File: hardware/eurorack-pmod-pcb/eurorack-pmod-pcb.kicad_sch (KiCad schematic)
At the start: 2 parts

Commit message: Finish schematic with AK4619, need to decide on other features
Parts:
- added C? (x2): 2u2, symbol Device:C_Polarized_Small
- added C? (x3): 10u, symbol Device:C_Polarized_Small
- added C? (x8): 1u, symbol Device:C_Polarized_Small
- added C? (x3): 100n, symbol Device:C_Small
- added J? (x7): PJ301BM, AudioJacks:Jack_3.5mm_QingPu_WQP-PJ301BM_Vertical, symbol Connector:AudioJack2_SwitchT
- added J?: PMOD_CONN, symbol Connector_Generic:Conn_02x06_Top_Bottom
- added JP?: OPEN, symbol Jumper:SolderJumper_2_Open
- added R? (x4): 33K, symbol Device:R
- added R? (x4): 68K, symbol Device:R
- added R? (x3): 4K7, symbol Device:R
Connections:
- net GND: now reaches J?.S
- net GND: now also U?.19 (VSS1), U?.2 (SDIN2), U?.20 (VREFL), U?.29 (SI), U?.33 (PAD), U?.4 (VSS2), C?.2, C?.2, C?.2, C?.2, C?.2, C?.2, C?.2, C?.2, J?.11 (Pin_11), J?.5 (Pin_5), J?.S, J?.S, J?.S, J?.S, J?.S, J?.S, J?.S, R?.2, R?.2, R?.2, R?.2, R?.2
- net at J?.T: now also R?.1
- net SDIN1: now reaches U?.1 (SDIN1)
- net SDIN1: now also J?.1 (Pin_1)
- net IN4_AUDIO_AC: now reaches U?.10 (IN4P/AIN4R/AIN6R)
- net IN4_AUDIO_AC: now also C?.1
- net IN3_AUDIO_AC: now reaches U?.12 (IN3P/AIN4L/AIN6L)
- net IN3_AUDIO_AC: now also C?.1
- net IN2_AUDIO_AC: now reaches U?.14 (IN2P/AIN1R/AIN3R)
- net IN2_AUDIO_AC: now also C?.1
- net IN1_AUDIO_AC: now reaches U?.16 (IN1P/AIN1L/AIN3L)
- net IN1_AUDIO_AC: now also C?.1
- net at U?.17 (VCOM): now also C?.1
- net +3V3: now reaches U?.18 (AVDD)
- net +3V3: now also U?.21 (VREFH), U?.3 (TVDD), C?.1, C?.1, C?.1, C?.1, C?.1, C?.1, J?.12 (Pin_12), J?.6 (Pin_6), JP?.1 (A), R?.1, R?.1
- net at U?.22 (AOUT1L): now also C?.2
- net at U?.23 (AOUT1R): now also C?.2
- net at U?.24 (AOUT2L): now also C?.2
- net at U?.25 (AOUT2R): now also C?.2
- net PDN: now reaches U?.26 (PDN)
- net PDN: now also J?.9 (Pin_9)
- net at U?.27 (CAD/~{CS}): now also JP?.2 (B), R?.1
- net SCL: now reaches U?.28 (SCL/SCLK)
- net SCL: now also J?.7 (Pin_7), R?.2
- net SDA: now reaches U?.30 (SDA/SO)
- net SDA: now also J?.8 (Pin_8), R?.2
- net SDOUT1: now reaches U?.31 (SDOUT1)
- net SDOUT1: now also J?.2 (Pin_2)
- net at U?.5 (AVDRV): now also C?.1
- net LRCK: now reaches U?.6 (LRCK)
- net LRCK: now also J?.3 (Pin_3)
- net BICK: now reaches U?.7 (BICK)
- net BICK: now also J?.4 (Pin_4)
- net MCLK: now reaches U?.8 (MCLK)
- net MCLK: now also J?.10 (Pin_10)
- new net: J?.T, R?.1 (x3)
- new net: C?.2, R?.1, R?.2 (x4)
- new net: C?.1, J?.T (x4)
- no-connect marks 0 -> 9
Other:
- moved on the sheet: J?, U?

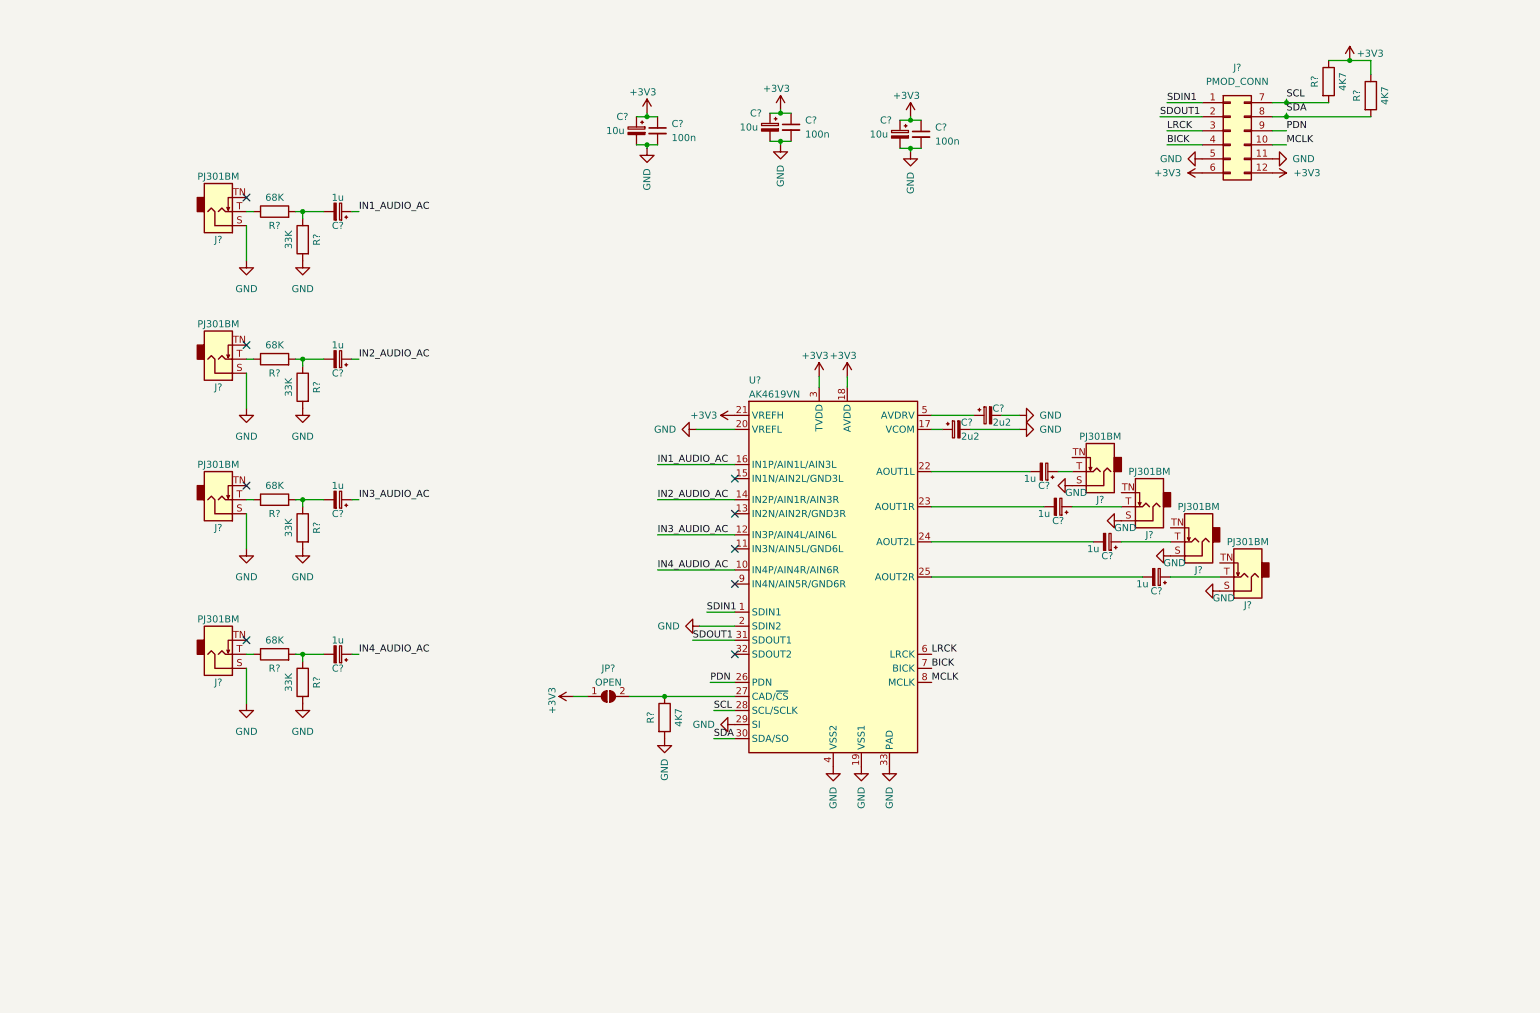
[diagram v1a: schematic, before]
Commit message: Finish input/output stages around AK4619
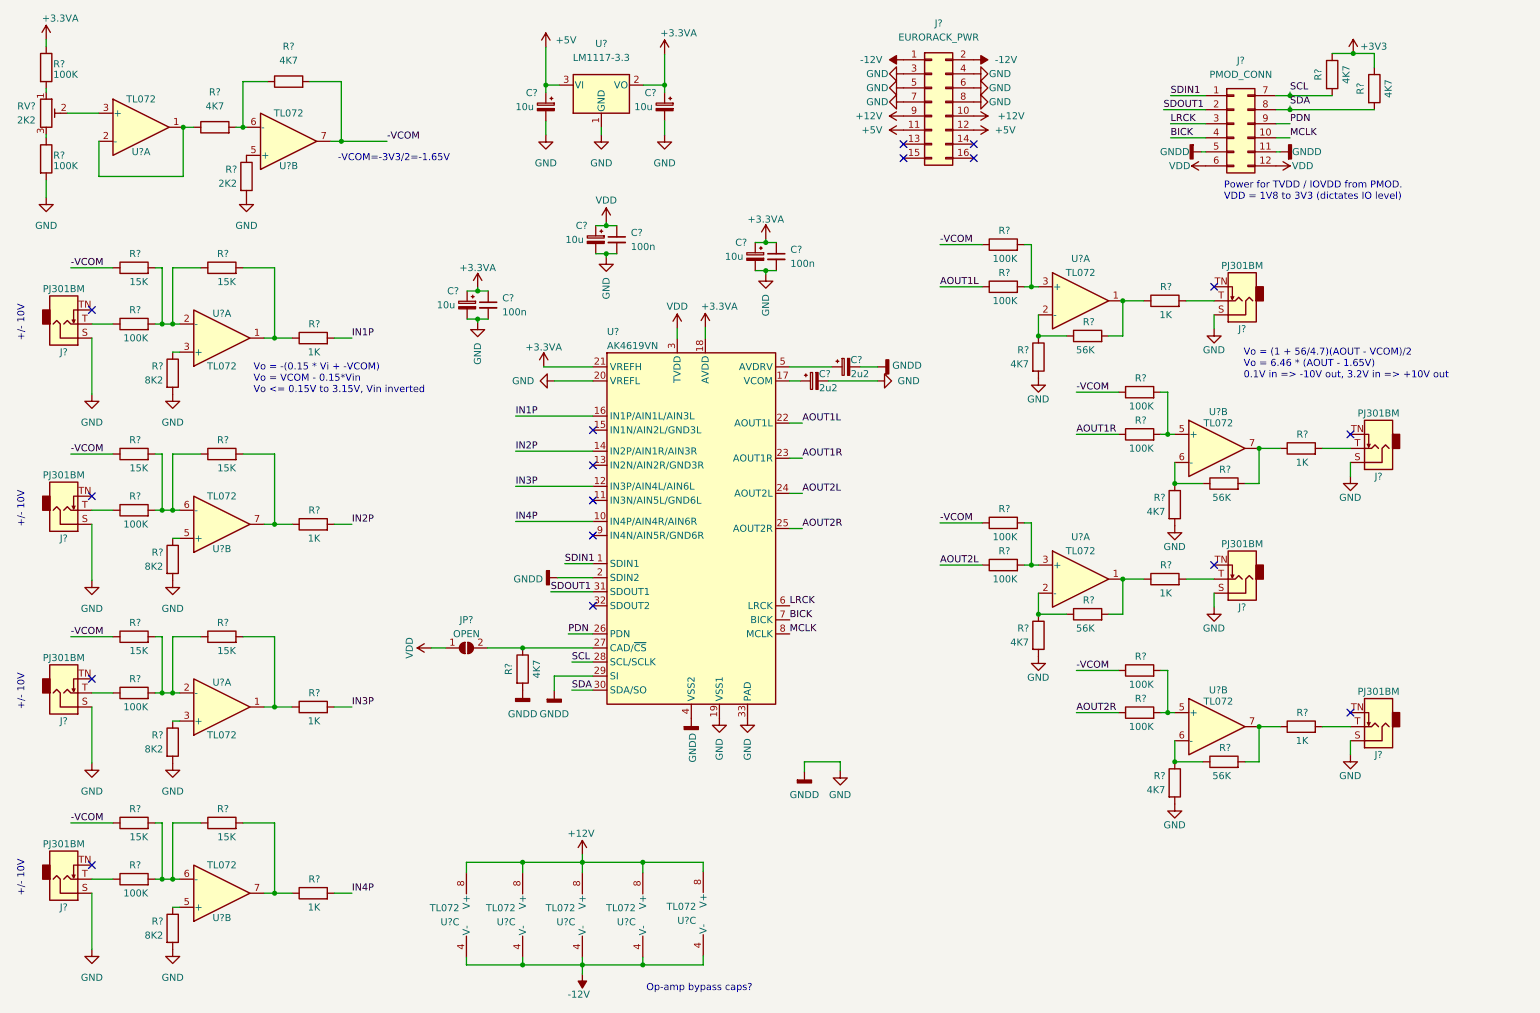
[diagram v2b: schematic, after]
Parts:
- removed C? (x8): 1u, symbol Device:C_Polarized_Small
- removed J? (x6): PJ301BM, AudioJacks:Jack_3.5mm_QingPu_WQP-PJ301BM_Vertical, symbol Connector:AudioJack2_SwitchT
- removed R? (x4): 33K, symbol Device:R
- removed R? (x4): 68K, symbol Device:R
- added C? (x2): 10u, symbol Device:C_Polarized_Small
- added J? (x6): PJ301BM, AudioJacks:Jack_3.5mm_QingPu_WQP-PJ301BM_Vertical, symbol Connector:AudioJack2_SwitchT
- added J?: EURORACK_PWR, symbol Connector_Generic:Conn_02x08_Odd_Even
- added R? (x8): 15K, symbol Device:R
- added R? (x14): 100K, symbol Device:R
- added R? (x8): 1K, symbol Device:R
- added R? (x6): 4K7, symbol Device:R
- added R? (x4): 8K2, symbol Device:R
- added R? (x4): 56K, symbol Device:R
- added R?: 2K2, symbol Device:R
- added RV?: 2K2, symbol Device:R_Potentiometer_Trim
- added U? (x15): TL072, symbol Amplifier_Operational:TL072
- added U?: LM1117-3.3, symbol Regulator_Linear:LM1117-3.3
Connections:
- net +3V3: no longer C?.1, C?.1, C?.1, C?.1, C?.1, C?.1, J?.12 (Pin_12), J?.6 (Pin_6), JP?.1 (A), U?.18 (AVDD), U?.21 (VREFH), U?.3 (TVDD)
- net GND: now also C?.2, C?.2, J?.3 (Pin_3), J?.4 (Pin_4), J?.5 (Pin_5), J?.6 (Pin_6), J?.7 (Pin_7), J?.8 (Pin_8), J?.S, J?.S, J?.S, J?.S, J?.S, J?.S, R?.2, R?.2, R?.2, R?.2, R?.2, R?.2, R?.2, R?.2, R?.2, R?.2, U?.1 (GND)
- net at J?.T: now also R?.1
- net AOUT2L: now reaches U?.24 (AOUT2L)
- net AOUT2L: now also R?.1
- net AOUT2R: now reaches U?.25 (AOUT2R)
- net AOUT2R: now also R?.1
- net at J?.T: now also R?.2
- net AOUT1L: now reaches U?.22 (AOUT1L)
- net AOUT1L: now also R?.1
- net AOUT1R: now reaches U?.23 (AOUT1R)
- net AOUT1R: now also R?.1
- net IN1_AUDIO_AC renamed IN1P
- net IN1P: now also R?.2
- net IN2_AUDIO_AC renamed IN2P
- net IN2P: now also R?.2
- net IN3_AUDIO_AC renamed IN3P
- net IN3P: now also R?.2
- net IN4_AUDIO_AC renamed IN4P
- net IN4P: now also R?.2
- new net: R?.1, U?.1, U?.2 (-)
- new net: RV?.2, U?.3 (+)
- new net: J?.T, R?.2 (x3)
- new net: R?.1, R?.2, R?.2, U?.2 (-) (x2)
- new net: R?.1, R?.2, U?.1 (x4)
- new net: R?.1, RV?.3
- new net: R?.2, RV?.1
- new net: J?.T, R?.1 (x3)
- new net: R?.1, R?.2, R?.2, U?.6 (-) (x2)
- new net: R?.1, U?.5 (+) (x3)
- new net: R?.1, R?.2, U?.7 (x4)
- new net: R?.2, R?.2, U?.5 (+) (x2)
- new net: R?.1, R?.1, U?.2 (-) (x2)
- new net: R?.1, R?.2, U?.6 (-)
- new net: R?.1, U?.3 (+) (x2)
- new net: R?.1, R?.1, U?.6 (-) (x2)
- new net: R?.2, R?.2, U?.3 (+) (x2)
- new net +12V: J?.10 (Pin_10), J?.9 (Pin_9), U?.8 (V+), U?.8 (V+), U?.8 (V+), U?.8 (V+), U?.8 (V+)
- new net +3.3VA: C?.1, C?.1, C?.1, C?.1, C?.1, R?.1, U?.18 (AVDD), U?.2 (VO), U?.21 (VREFH)
- new net +5V: C?.1, J?.11 (Pin_11), J?.12 (Pin_12), U?.3 (VI)
- new net -12V: J?.1 (Pin_1), J?.2 (Pin_2), U?.4 (V-), U?.4 (V-), U?.4 (V-), U?.4 (V-), U?.4 (V-)
- new net -VCOM: R?.1, R?.1, R?.1, R?.1, R?.1, R?.1, R?.1, R?.1, R?.2, U?.7
- new net VDD: C?.1, C?.1, J?.12 (Pin_12), J?.6 (Pin_6), JP?.1 (A), U?.3 (TVDD)
- no-connect marks 9 -> 17
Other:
- note added: "+/- 10V"
- note added: "-VCOM=-3V3/2=-1.65V"
- note added: "Op-amp bypass caps?"
- note added: "Power for TVDD / IOVDD from PMOD. VDD = 1V8 to 3V3 (dictates IO level)"
- note added: "Vo = (1 + 56/4.7)(AOUT - VCOM)/2 Vo = 6.46 * (AOUT - 1.65V) 0.1V in => -10V out, 3.2V in => +10V out"
- note added: "Vo = -(0.15 * Vi + -VCOM) Vo = VCOM - 0.15*Vin Vo <= 0.15V to 3.15V, Vin inverted"
- moved on the sheet: C?, J?, JP?, R?, U?

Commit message: Annotate and assign easy footprints
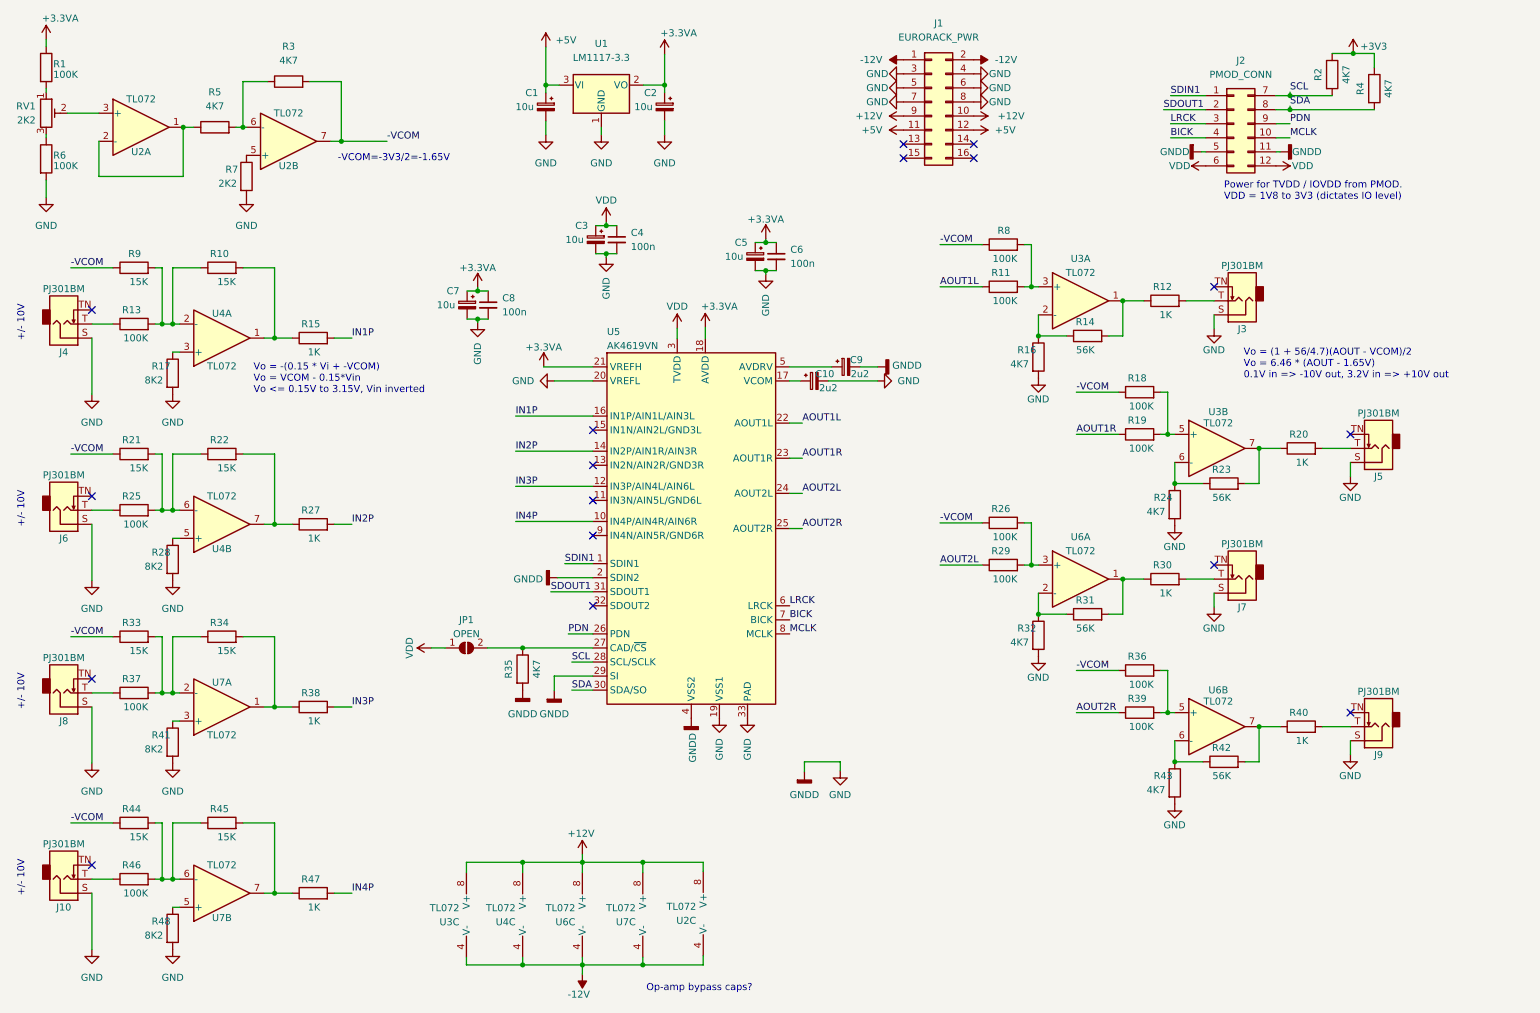
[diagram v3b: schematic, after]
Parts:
- C4, C6, C8: renamed from C?; footprint (none) -> Capacitor_SMD:C_0603_1608Metric
- JP1: renamed from JP?; footprint (none) -> Resistor_SMD:R_0603_1608Metric
- R1, R10, R11, R12, R13, R14, R15, R16, R17, R18, R19, R2, R20, R21, R22, R23, R24, R25, R26, R27, R28, R29, R3, R30, R31, R32, R33, R34, R35, R36, R37, R38, R39, R4, R40, R41, R42, R43, R44, R45, R46, R47, R48, R5, R6, R7, R8, R9: renamed from R?; footprint (none) -> Resistor_SMD:R_0603_1608Metric
- U1: renamed from U?; footprint (none) -> Package_TO_SOT_SMD:SOT-223-3_TabPin2
- U2, U3, U4, U6, U7: renamed from U?; footprint (none) -> Package_SO:SOIC-8_3.9x4.9mm_P1.27mm
- gave numbers to parts that had none: 19

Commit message: Finish schematic capture, ERC, footprints
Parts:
- removed J10, J3, J4, J5, J6, J7, J8, J9: PJ301BM, AudioJacks:Jack_3.5mm_QingPu_WQP-PJ301BM_Vertical, symbol Connector:AudioJack2_SwitchT
- removed J2: PMOD_CONN, symbol Connector_Generic:Conn_02x06_Top_Bottom
- removed JP1: OPEN, Resistor_SMD:R_0603_1608Metric, symbol Jumper:SolderJumper_2_Open
- removed R11, R13, R18, R19, R25, R26, R29, R36, R37, R39, R46: 100K, Resistor_SMD:R_0603_1608Metric, symbol Device:R
- removed R12, R15, R20, R27, R30, R38, R40, R47: 1K, Resistor_SMD:R_0603_1608Metric, symbol Device:R
- removed R14, R23, R31, R42: 56K, Resistor_SMD:R_0603_1608Metric, symbol Device:R
- removed R16, R24, R32, R43: 4K7, Resistor_SMD:R_0603_1608Metric, symbol Device:R
- removed R17, R28, R41, R48: 8K2, Resistor_SMD:R_0603_1608Metric, symbol Device:R
- removed R21, R22, R33, R34, R44, R45, R9: 15K, Resistor_SMD:R_0603_1608Metric, symbol Device:R
- removed RV1: 2K2, symbol Device:R_Potentiometer_Trim
- removed unit 3 of U2
- removed U3, U4, U7: TL072, Package_SO:SOIC-8_3.9x4.9mm_P1.27mm, symbol Amplifier_Operational:TL072
- removed unit 1 of U6
- removed unit 2 of U6
- added C11, C13, C15, C17: 10u, Capacitor_Tantalum_SMD:CP_EIA-3216-10_Kemet-I, symbol Device:C_Polarized_Small
- added C12, C14, C16, C18: 100n, Capacitor_SMD:C_0603_1608Metric, symbol Device:C_Small
- added J1: OPTIONAL, Connector_PinHeader_2.54mm:PinHeader_2x04_P2.54mm_Vertical, symbol Connector_Generic:Conn_02x04_Odd_Even
- added J2: PMOD, Connector_PinHeader_2.54mm:PinHeader_2x06_P2.54mm_Vertical, symbol Connector_Generic:Conn_02x06_Odd_Even
- C1, C10, C2, C9: footprint (none) -> Capacitor_Tantalum_SMD:CP_EIA-3216-10_Kemet-I
- C3: renamed from C7; footprint (none) -> Capacitor_Tantalum_SMD:CP_EIA-3216-10_Kemet-I
- C5: renamed from C3; footprint (none) -> Capacitor_Tantalum_SMD:CP_EIA-3216-10_Kemet-I
- C7: renamed from C5; footprint (none) -> Capacitor_Tantalum_SMD:CP_EIA-3216-10_Kemet-I
- J3: renamed from J1; footprint (none) -> Connector_PinHeader_2.54mm:PinHeader_2x08_P2.54mm_Vertical
- R10: value 15K -> 4K7
- R8: value 100K -> 4K7
- renumbered C8 to C4, C4 to C6, C6 to C8, R2 to R1, R4 to R2, R1 to R3, R3 to R4, R35 to R9, U6 to U2, U5 to U3
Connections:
- net +3V3 is gone; now on net VDD: R1.1, R2.1
- net +12V: now also C11.1, C12.1, C13.1, C14.1
- net +3.3VA: now also J1.5 (Pin_5)
- net -12V: now also C15.2, C16.2, C17.2, C18.2
- net -VCOM: no longer R8.1
- net BICK: now also J2.7 (Pin_7)
- net GND: now also R10.2, R8.2, C11.2, C12.2, C13.2, C14.2, C15.1, C16.1, C17.1, C18.1, J1.7 (Pin_7), J1.8 (Pin_8), J2.10 (Pin_10), J2.9 (Pin_9); no longer U3.2 (SDIN2), U3.29 (SI)
- net LRCK: now also J2.5 (Pin_5)
- net MCLK: now also J2.8 (Pin_8)
- net PDN: now also J2.6 (Pin_6)
- net SCL: now also J2.2 (Pin_2)
- net SDA: now also J2.4 (Pin_4)
- net SDIN1: now also J2.1 (Pin_1)
- net SDOUT1: now also J2.3 (Pin_3)
- net VDD: now also J1.6 (Pin_6), J2.11 (Pin_11), J2.12 (Pin_12)
- net at U2.3 (+): now also R3.2, R6.1
- net SI: now reaches R10.1
- net SI: now also U3.29 (SI), J1.2 (Pin_2)
- net CAD/~{CS}: now reaches R9.1, U3.27 (CAD/~{CS})
- net CAD/~{CS}: now also J1.4 (Pin_4)
- net SDOUT2: now reaches U3.32 (SDOUT2)
- net SDOUT2: now also J1.3 (Pin_3)
- net AOUT1L renamed dual_mono_outputs1/OUT1
- net AOUT1R renamed dual_mono_outputs1/OUT2
- net AOUT2L renamed dual_mono_outputs2/OUT1
- net AOUT2R renamed dual_mono_outputs2/OUT2
- net IN1P renamed dual_mono_inputs1/IN1_3V
- net IN2P renamed dual_mono_inputs1/IN2_3V
- net IN3P renamed dual_mono_inputs2/IN1_3V
- net IN4P renamed dual_mono_inputs2/IN2_3V
- new net SDIN2: J1.1 (Pin_1), R8.1, U3.2 (SDIN2)
- no-connect marks 17 -> 8
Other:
- added sheet dual_mono_inputs1 (dual_mono_inputs.kicad_sch)
- added sheet dual_mono_inputs2 (dual_mono_inputs.kicad_sch)
- added sheet dual_mono_outputs1 (dual_mono_outputs.kicad_sch)
- added sheet dual_mono_outputs2 (dual_mono_outputs.kicad_sch)
- note removed: "+/- 10V"
- note removed: "Op-amp bypass caps?"
- note removed: "Vo = (1 + 56/4.7)(AOUT - VCOM)/2 Vo = 6.46 * (AOUT - 1.65V) 0.1V in => -10V out, 3.2V in => +10V out"
- note removed: "Vo = -(0.15 * Vi + -VCOM) Vo = VCOM - 0.15*Vin Vo <= 0.15V to 3.15V, Vin inverted"
- moved on the sheet: C1, C10, C2, C3, C4, C5, C6, C7, C8, C9, J3, R1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
